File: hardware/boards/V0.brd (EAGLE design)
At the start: 139 parts, among them IC2 TPS6300, J1 SJ-43515TS-SMT, J2 HIROSE_DM3BT-DSF-PEJSHIROSE_D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, J3 MOLEX_105450-0101MOLEX_105450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, Q2 ON_SEMI_MMBT5551LT1GON_SEMI_M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, U1 VS1053-L, U2 MICROCHIP_MCP73831T-2ATI-OTMI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, X3 FH12-45S-0.5SH

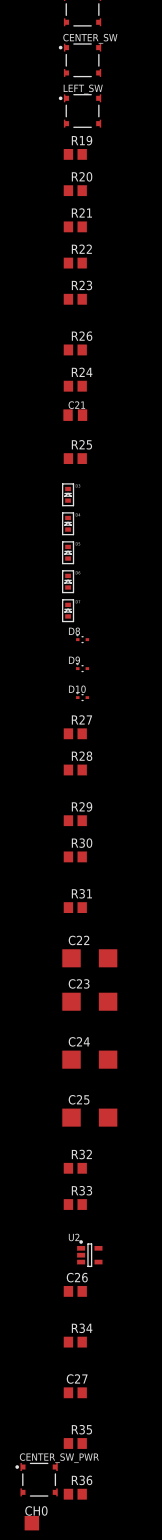
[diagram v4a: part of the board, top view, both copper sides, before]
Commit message: Swap center buttons for 100Q (lower actuation force) variants
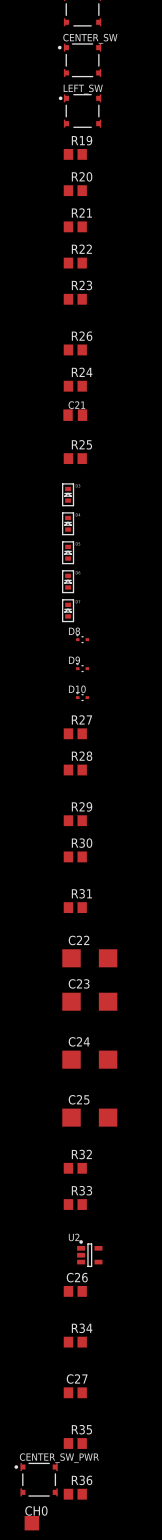
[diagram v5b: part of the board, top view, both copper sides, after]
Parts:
- CENTER_SW, CENTER_SW_PWR: value E-SWITCH_TL3315NF160QE-SWITCH_TL3315NF160Q_0_0 -> E-SWITCH_TL3315NF100QE-SWITCH_TL3315NF100Q_0_0; device E-Switch-TL3315NF160Q:E-SWITCH_TL3315NF160Q_0 -> E-Switch-TL3315NF100Q:E-SWITCH_TL3315NF100Q_0
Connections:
- net CENTER_SW renamed N$44
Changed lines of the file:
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@@
 <attribute name="TEMPERATURE_RANGE_LOW" value="-20°C" x="-41" y="-357" size="1.778" layer="27" display="off"/>
 </element>
-<element name="CENTER_SW" library="E-Switch-TL3315NF160Q" package="E-SWITCH_TL3315NF160Q_0" value="E-SWITCH_TL3315NF160QE-SWITCH_TL3315NF160Q_0_0" x="-35" y="-371" smashed="yes">
+<element name="CENTER_SW" library="E-Switch-TL3315NF100Q" package="E-SWITCH_TL3315NF100Q_0" value="E-SWITCH_TL3315NF100QE-SWITCH_TL3315NF100Q_0_0" x="-35" y="-371" smashed="yes">
 <attribute name="CENTROID_NOT_SPECIFIED" value="No" x="-41" y="-364" size="1.778" layer="27" display="off"/>
-<attribute name="DATASHEET" value="http://media.digikey.com/pdf/Data%20Sheets/E-Switch%20PDFs/TL3315.pdf" x="-41" y="-364" size="1.778" layer="27" display="off"/>
-<attribute name="DIGIKEY_DESCRIPTION" value="SWITCH TACTILE SPST-NO 0.05A 15V" x="-41" y="-364" size="1.778" layer="27" display="off"/>
-<attribute name="DIGIKEY_PART_NUMBER" value="EG4621CT-ND" x="-41" y="-364" size="1.778" layer="27" display="off"/>
+<attribute name="CIRCUIT" value="SPST-NO" x="-35" y="-371" size="1.778" layer="27" display="off"/>
+<attribute name="CONTACT_RATING_@_VOLTAGE" value="0.05A @ 15VDC" x="-35" y="-371" size="1.778" layer="27" display="off"/>
+<attribute name="DATASHEET" value="http://spec_sheets.e-switch.com/specs/P010336.pdf" x="-41" y="-364" size="1.778" layer="27" display="off"/>
+<attribute name="DIGIKEY_DESCRIPTION" value="SWITCH Tactile Switch SPST-NO Top Actuated Surface Mount" x="-41" y="-364" size="1.778" layer="27" display="off"/>
+<attribute name="DIGIKEY_PART_NUMBER" value="EG4620CT-ND" x="-41" y="-364" size="1.778" layer="27" display="off"/>
 <attribute name="LEAD_FREE" value="yes" x="-41" y="-364" size="1.778" layer="27" display="off"/>
 <attribute name="MF" value="E-Switch" x="-41" y="-364" size="1.778" layer="27" display="off"/>
-<attribute name="MOUSER_PART_NUMBER" value="612-TL3315NF160Q" x="-41" y="-364" size="1.778" layer="27" display="off"/>
-<attribute name="MPN" value="TL3315NF160Q" x="-41" y="-364" size="1.778" layer="27" display="off"/>
+<attribute name="MOUSER_PART_NUMBER" value="612-TL3315NF100Q" x="-41" y="-364" size="1.778" layer="27" display="off"/>
+<attribute name="MPN" value="TL3315NF100Q" x="-41" y="-364" size="1.778" layer="27" display="off"/>
 <attribute name="NAME" x="-37.725" y="-368.375" size="1" layer="25"/>
-<attribute name="PACKAGE" value="SW_SMT_4MM5_4MM5" x="-41" y="-364" size="1.778" layer="27" display="off"/>
+<attribute name="PACKAGE" value="SMT_4POS" x="-41" y="-364" size="1.778" layer="27" display="off"/>
 <attribute name="PREFIX" value="SW" x="-41" y="-364" size="1.778" layer="27" display="off"/>
 <attribute name="ROHS" value="yes" x="-41" y="-364" size="1.778" layer="27" display="off"/>
@@
 <attribute name="VALUE" x="-36.635" y="-571.54" size="1.27" layer="27"/>
 </element>
-<element name="CENTER_SW_PWR" library="E-Switch-TL3315NF160Q" package="E-SWITCH_TL3315NF160Q_0" value="E-SWITCH_TL3315NF160QE-SWITCH_TL3315NF160Q_0_0" x="-41" y="-567" smashed="yes">
+<element name="CENTER_SW_PWR" library="E-Switch-TL3315NF100Q" package="E-SWITCH_TL3315NF100Q_0" value="E-SWITCH_TL3315NF100QE-SWITCH_TL3315NF100Q_0_0" x="-41" y="-567" smashed="yes">
 <attribute name="CENTROID_NOT_SPECIFIED" value="No" x="-41" y="-567" size="1.778" layer="27" display="off"/>
-<attribute name="DATASHEET" value="http://media.digikey.com/pdf/Data%20Sheets/E-Switch%20PDFs/TL3315.pdf" x="-41" y="-567" size="1.778" layer="27" display="off"/>
-<attribute name="DIGIKEY_DESCRIPTION" value="SWITCH TACTILE SPST-NO 0.05A 15V" x="-41" y="-567" size="1.778" layer="27" display="off"/>
-<attribute name="DIGIKEY_PART_NUMBER" value="EG4621CT-ND" x="-41" y="-567" size="1.778" layer="27" display="off"/>
+<attribute name="CIRCUIT" value="SPST-NO" x="-41" y="-567" size="1.778" layer="27" display="off"/>
+<attribute name="CONTACT_RATING_@_VOLTAGE" value="0.05A @ 15VDC" x="-41" y="-567" size="1.778" layer="27" display="off"/>
+<attribute name="DATASHEET" value="http://spec_sheets.e-switch.com/specs/P010336.pdf" x="-41" y="-567" size="1.778" layer="27" display="off"/>
+<attribute name="DIGIKEY_DESCRIPTION" value="SWITCH Tactile Switch SPST-NO Top Actuated Surface Mount" x="-41" y="-567" size="1.778" layer="27" display="off"/>
+<attribute name="DIGIKEY_PART_NUMBER" value="EG4620CT-ND" x="-41" y="-567" size="1.778" layer="27" display="off"/>
 <attribute name="LEAD_FREE" value="yes" x="-41" y="-567" size="1.778" layer="27" display="off"/>
 <attribute name="MF" value="E-Switch" x="-41" y="-567" size="1.778" layer="27" display="off"/>
-<attribute name="MOUSER_PART_NUMBER" value="612-TL3315NF160Q" x="-41" y="-567" size="1.778" layer="27" display="off"/>
-<attribute name="MPN" value="TL3315NF160Q" x="-41" y="-567" size="1.778" layer="27" display="off"/>
+<attribute name="MOUSER_PART_NUMBER" value="612-TL3315NF100Q" x="-41" y="-567" size="1.778" layer="27" display="off"/>
+<attribute name="MPN" value="TL3315NF100Q" x="-41" y="-567" size="1.778" layer="27" display="off"/>
 <attribute name="NAME" x="-43.725" y="-564.375" size="1" layer="25"/>
-<attribute name="PACKAGE" value="SW_SMT_4MM5_4MM5" x="-41" y="-567" size="1.778" layer="27" display="off"/>
+<attribute name="PACKAGE" value="SMT_4POS" x="-41" y="-567" size="1.778" layer="27" display="off"/>
 <attribute name="PREFIX" value="SW" x="-41" y="-567" size="1.778" layer="27" display="off"/>
 <attribute name="ROHS" value="yes" x="-41" y="-567" size="1.778" layer="27" display="off"/>
@@
 <contactref element="DOWN_SW" pad="2-2"/>
 <contactref element="DOWN_SW" pad="2"/>
-<contactref element="CENTER_SW" pad="2-2"/>
-<contactref element="CENTER_SW" pad="2"/>
 <contactref element="C21" pad="1"/>
 <contactref element="D1" pad="2"/>
@@
 <contactref element="X3" pad="33"/>
 <contactref element="X3" pad="31"/>
+<contactref element="CENTER_SW" pad="2"/>
+<contactref element="CENTER_SW" pad="2-2"/>
 <wire x1="-24.075" y1="-200.0822" x2="-23.475" y2="-222.175" width="0" layer="19" extent="1-1"/>
 <wire x1="-26.025" y1="-200.0822" x2="-24.075" y2="-200.0822" width="0" layer="19" extent="1-1"/>
@@
 <wire x1="-32.525" y1="-362.25" x2="-32.525" y2="-355.25" width="0" layer="19" extent="1-1"/>
 <wire x1="-32.875" y1="-362.25" x2="-32.525" y2="-362.25" width="0" layer="19" extent="1-1"/>
-<wire x1="-32.525" y1="-369.25" x2="-32.525" y2="-362.25" width="0" layer="19" extent="1-1"/>
-<wire x1="-32.875" y1="-369.25" x2="-32.525" y2="-369.25" width="0" layer="19" extent="1-1"/>
-<wire x1="-32.525" y1="-376.25" x2="-32.525" y2="-369.25" width="0" layer="19" extent="1-1"/>
+<wire x1="-32.875" y1="-369.25" x2="-32.525" y2="-362.25" width="0" layer="19" extent="1-1"/>
+<wire x1="-32.525" y1="-369.25" x2="-32.875" y2="-369.25" width="0" layer="19" extent="1-1"/>
+<wire x1="-32.525" y1="-376.25" x2="-32.875" y2="-369.25" width="0" layer="19" extent="1-1"/>
 <wire x1="-32.875" y1="-376.25" x2="-32.525" y2="-376.25" width="0" layer="19" extent="1-1"/>
 <wire x1="-5.7" y1="-331" x2="-7.05" y2="-315" width="0" layer="19" extent="1-1"/>
@@
 <wire x1="-32.525" y1="-365.75" x2="-32.875" y2="-365.75" width="0" layer="19" extent="1-1"/>
 </signal>
-<signal name="CENTER_SW">
-<contactref element="CENTER_SW" pad="4-2"/>
-<contactref element="CENTER_SW" pad="4"/>
-<contactref element="R23" pad="2"/>
-<contactref element="D7" pad="A"/>
-<wire x1="-35.05" y1="-404" x2="-37" y2="-447.8" width="0" layer="19" extent="1-1"/>
-<wire x1="-32.875" y1="-372.75" x2="-35.05" y2="-404" width="0" layer="19" extent="1-1"/>
-<wire x1="-32.525" y1="-372.75" x2="-32.875" y2="-372.75" width="0" layer="19" extent="1-1"/>
-</signal>
 <signal name="USB_D+">
 <contactref element="JL" pad="P$4"/>
@@
 <wire x1="-25.05" y1="-265.075" x2="-40.05" y2="-803.1" width="0" layer="19" extent="1-1"/>
 </signal>
+<signal name="N$44">
+<contactref element="D7" pad="A"/>
+<contactref element="CENTER_SW" pad="4-2"/>
+<contactref element="CENTER_SW" pad="4"/>
+<contactref element="R23" pad="2"/>
+<wire x1="-35.05" y1="-404" x2="-37" y2="-447.8" width="0" layer="19" extent="1-1"/>
+<wire x1="-32.875" y1="-372.75" x2="-35.05" y2="-404" width="0" layer="19" extent="1-1"/>
+<wire x1="-32.525" y1="-372.75" x2="-32.875" y2="-372.75" width="0" layer="19" extent="1-1"/>
+</signal>
 </signals>

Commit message: add missing esp32 capacitor values
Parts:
- C32: value (none) -> 10uF
- C33: value (none) -> 0.1uF
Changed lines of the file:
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@@
 <attribute name="VALUE" x="-42.635" y="-754.54" size="1.27" layer="27"/>
 </element>
-<element name="C32" library="rcl" library_urn="urn:adsk.eagle:library:334" package="C1206" package3d_urn="urn:adsk.eagle:package:23618/2" value="" x="-41" y="-759" smashed="yes">
+<element name="C32" library="rcl" library_urn="urn:adsk.eagle:library:334" package="C1206" package3d_urn="urn:adsk.eagle:package:23618/2" value="10uF" x="-41" y="-759" smashed="yes">
 <attribute name="NAME" x="-42.27" y="-757.73" size="1.27" layer="25"/>
 <attribute name="SPICEPREFIX" value="C" x="-41" y="-759" size="1.778" layer="27" display="off"/>
 <attribute name="VALUE" x="-42.27" y="-761.54" size="1.27" layer="27"/>
 </element>
-<element name="C33" library="rcl" library_urn="urn:adsk.eagle:library:334" package="C1206" package3d_urn="urn:adsk.eagle:package:23618/2" value="" x="-41" y="-764" smashed="yes">
+<element name="C33" library="rcl" library_urn="urn:adsk.eagle:library:334" package="C1206" package3d_urn="urn:adsk.eagle:package:23618/2" value="0.1uF" x="-41" y="-764" smashed="yes">
 <attribute name="NAME" x="-42.27" y="-762.73" size="1.27" layer="25"/>
 <attribute name="SPICEPREFIX" value="C" x="-41" y="-764" size="1.778" layer="27" display="off"/>

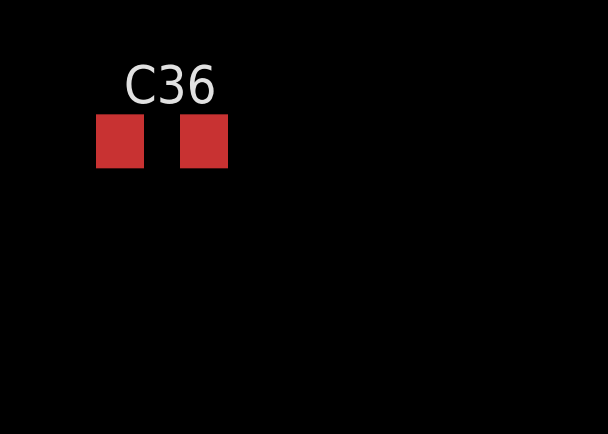
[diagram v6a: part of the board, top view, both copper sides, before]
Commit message: Add charge detect back in, using up all our pins
Closes #11
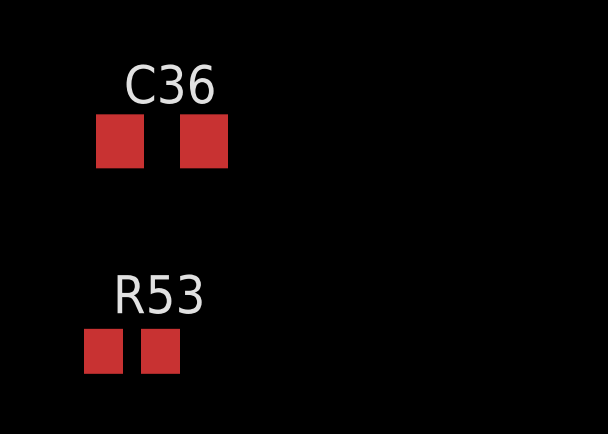
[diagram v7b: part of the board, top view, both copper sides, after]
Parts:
- added R53: 10k, rcl:R0805
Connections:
- new net CHARGE_DETECT: R53.1, U$1.6
- net RED_LED_CATH: now also R53.2
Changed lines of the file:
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@@
 <attribute name="VALUE" x="-42.27" y="-811.54" size="1.27" layer="27"/>
+</element>
+<element name="R53" library="rcl" library_urn="urn:adsk.eagle:library:334" package="R0805" package3d_urn="urn:adsk.eagle:package:23553/2" value="10k" x="-42" y="-816" smashed="yes">
+<attribute name="NAME" x="-42.635" y="-814.73" size="1.27" layer="25"/>
+<attribute name="SPICEPREFIX" value="R" x="-42" y="-816" size="1.778" layer="27" display="off"/>
+<attribute name="VALUE" x="-42.635" y="-818.54" size="1.27" layer="27"/>
 </element>
 </elements>
@@
 <contactref element="R35" pad="2"/>
 <contactref element="U2" pad="1"/>
+<contactref element="R53" pad="2"/>
+<wire x1="-35.05" y1="-562" x2="-41.05" y2="-816" width="0" layer="19" extent="1-1"/>
 <wire x1="-35.2" y1="-535.05" x2="-35.05" y2="-562" width="0" layer="19" extent="1-1"/>
 </signal>
@@
 <wire x1="-32.525" y1="-372.75" x2="-32.875" y2="-372.75" width="0" layer="19" extent="1-1"/>
 </signal>
+<signal name="CHARGE_DETECT">
+<contactref element="R53" pad="1"/>
+<contactref element="U$1" pad="6"/>
+<wire x1="-21.275" y1="-6.75" x2="-42.95" y2="-816" width="0" layer="19" extent="1-1"/>
+</signal>
 </signals>

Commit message: checkpoint
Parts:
- moved R53 919.8 mm to (138.0, 86.0), turned to 90 degrees
- moved C36 912.4 mm to (131.0, 87.0), turned to 90 degrees
- moved G1 904.2 mm to (124.0, 87.0), turned to 90 degrees
- moved R49 846.0 mm to (74.0, 86.0), turned to 90 degrees
- moved R48 840.4 mm to (69.0, 86.0), turned to 90 degrees
- moved Q3 834.5 mm to (63.0, 87.0), turned to 90 degrees
- moved Q1 822.7 mm to (56.0, 82.0), turned to 90 degrees
- moved R47 819.2 mm to (50.0, 86.0), turned to 90 degrees
- moved R46 811.5 mm to (43.0, 86.0), turned to 90 degrees
- moved TP8 805.1 mm to (38.0, 85.0), turned to 90 degrees
- moved R52 804.8 mm to (-8.23, 9.06), flipped to the bottom, turned to 90 degrees
- moved TP7 799.6 mm to (33.0, 85.0), turned to 90 degrees
- moved R51 795.3 mm to (-8.23, 4.57), flipped to the bottom, turned to 90 degrees
- moved TP6 794.2 mm to (28.0, 85.0), turned to 90 degrees
- moved C35 793.6 mm to (-12.0, 10.0), flipped to the bottom
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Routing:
- net VBAT: track 0.00 -> 16.0 mm
- net V3P3: track 0.00 -> 12.2 mm, vias 0 -> 2
- net N$42: track 0.00 -> 10.6 mm
- net V1P8: track 0.00 -> 10.1 mm
- net VBUS: track 0.00 -> 8.12 mm, vias 0 -> 2
- net N$51: track 0.00 -> 4.10 mm, vias 0 -> 2
- net N$17: track 0.00 -> 3.56 mm
- net N$50: track 0.00 -> 3.12 mm
- net N$13: track 0.00 -> 2.85 mm
- net N$2: track 0.00 -> 2.64 mm
- net N$15: track 0.00 -> 2.58 mm
- net N$9: track 0.00 -> 2.56 mm
- net N$7: track 0.00 -> 2.48 mm
- net EN: track 0.00 -> 2.29 mm
- net USB_D-: track 0.00 -> 1.94 mm, vias 0 -> 2
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- added copper zone on layer 1, net GND
- added copper zone on layer 16, net GND
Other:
- board outline added: 45 x 104.5 mm
- board text added: "2mm should be enough to account for the 0.5mm tolerance, the bend, and going through the hole"
- board text added: "<- Display ->"
